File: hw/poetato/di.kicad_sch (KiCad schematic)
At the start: 10 parts, among them Q3 NTK3134N, U12 ISO1211

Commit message: hw: sync symbols with kicadlib field text and value updates
Update Symbols from Library for kicadlib 8686346 (field text 1.27 mm) and
5b35b6c (units on misc R/C values). Value text sizes synced to the library
by script, since a Value reset would also reset power-symbol net names.
Restored BOM_Entry Manufacturer/Part Number and the R57 Power field that the
update cleared, and field positions it reset. Nudged R1, C6, Q6 and C75 text
clear of the larger power-symbol labels. ERC clean, netlist unchanged apart
from the intended values.
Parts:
- R57: value 1k -> 1kΩ
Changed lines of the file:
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@@
 			(effects
 				(font
-					(size 1.524 1.524)
+					(size 1.27 1.27)
 				)
 				(justify left)
@@
 			(effects
 				(font
-					(size 1.524 1.524)
+					(size 1.27 1.27)
 				)
 				(justify left)
@@
 		(dnp no)
 		(fields_autoplaced yes)
-		(property "Reference" "#PWR094"
+		(property "Reference" "#PWR94"
 			(at 96.52 159.766 0)
 			(hide yes)
@@
 			(effects
 				(font
-					(size 0.508 0.508)
+					(size 1.27 1.27)
 				)
 			)
@@
 			(effects
 				(font
-					(size 0.762 0.762)
+					(size 1.27 1.27)
 				)
 			)
@@
 			(effects
 				(font
-					(size 1.524 1.524)
+					(size 1.27 1.27)
 				)
 			)
@@
 			(effects
 				(font
-					(size 1.524 1.524)
+					(size 1.27 1.27)
 				)
 			)
@@
 			(project "poetato"
 				(path "/f0f504bb-124c-46e5-ad39-032d3dfa78b3/7f50897c-81bd-4425-95ed-f5153c9db421/32a242c7-d9b1-4608-861e-d6aa3d0d20fd"
-					(reference "#PWR098")
+					(reference "#PWR98")
 					(unit 1)
 				)
 				(path "/f0f504bb-124c-46e5-ad39-032d3dfa78b3/7f50897c-81bd-4425-95ed-f5153c9db421/3e09c94c-e2ca-4383-a1d9-a605e5d78e01"
-					(reference "#PWR094")
+					(reference "#PWR94")
 					(unit 1)
 				)
 				(path "/f0f504bb-124c-46e5-ad39-032d3dfa78b3/7f50897c-81bd-4425-95ed-f5153c9db421/4efb7764-a312-4e2a-a696-e9a56a5b9d5e"
-					(reference "#PWR096")
+					(reference "#PWR96")
 					(unit 1)
 				)
@@
 		(in_pos_files yes)
 		(dnp no)
+		(fields_autoplaced yes)
 		(property "Reference" "R57"
 			(at 180.34 85.09 90)
@@
 			)
 		)
-		(property "Value" "1k"
+		(property "Value" "1kΩ"
 			(at 180.34 87.63 90)
 			(show_name no)
@@
 		(dnp no)
 		(fields_autoplaced yes)
-		(property "Reference" "#PWR0120"
+		(property "Reference" "#PWR120"
 			(at 96.52 88.646 0)
 			(hide yes)
@@
 			(effects
 				(font
-					(size 0.508 0.508)
+					(size 1.27 1.27)
 				)
 			)
@@
 			(effects
 				(font
-					(size 0.762 0.762)
+					(size 1.27 1.27)
 				)
 			)
@@
 			(effects
 				(font
-					(size 1.524 1.524)
+					(size 1.27 1.27)
 				)
 			)
@@
 			(effects
 				(font
-					(size 1.524 1.524)
+					(size 1.27 1.27)
 				)
 			)
@@
 			(project "poetato"
 				(path "/f0f504bb-124c-46e5-ad39-032d3dfa78b3/7f50897c-81bd-4425-95ed-f5153c9db421/32a242c7-d9b1-4608-861e-d6aa3d0d20fd"
-					(reference "#PWR0157")
+					(reference "#PWR157")
 					(unit 1)
 				)
 				(path "/f0f504bb-124c-46e5-ad39-032d3dfa78b3/7f50897c-81bd-4425-95ed-f5153c9db421/3e09c94c-e2ca-4383-a1d9-a605e5d78e01"
-					(reference "#PWR0120")
+					(reference "#PWR120")
 					(unit 1)
 				)
 				(path "/f0f504bb-124c-46e5-ad39-032d3dfa78b3/7f50897c-81bd-4425-95ed-f5153c9db421/4efb7764-a312-4e2a-a696-e9a56a5b9d5e"
-					(reference "#PWR0129")
+					(reference "#PWR129")
 					(unit 1)
 				)
@@
 			(effects
 				(font
-					(size 0.9906 0.9906)
+					(size 1.27 1.27)
 				)
 				(justify left)
@@
 			(effects
 				(font
-					(size 1.016 1.016)
+					(size 1.27 1.27)
 				)
 				(justify left)
@@
 			(effects
 				(font
-					(size 0.9906 0.9906)
+					(size 1.27 1.27)
 				)
 				(justify left)
@@
 		(dnp no)
 		(fields_autoplaced yes)
-		(property "Reference" "#PWR082"
+		(property "Reference" "#PWR82"
 			(at 111.76 106.426 0)
 			(hide yes)
@@
 			(effects
 				(font
-					(size 0.508 0.508)
+					(size 1.27 1.27)
 				)
 			)
@@
 			(effects
 				(font
-					(size 0.762 0.762)
+					(size 1.27 1.27)
 				)
 			)
@@
 			(effects
 				(font
-					(size 1.524 1.524)
+					(size 1.27 1.27)
 				)
 			)
@@
 			(effects
 				(font
-					(size 1.524 1.524)
+					(size 1.27 1.27)
 				)
 			)
@@
 			(project "poetato"
 				(path "/f0f504bb-124c-46e5-ad39-032d3dfa78b3/7f50897c-81bd-4425-95ed-f5153c9db421/32a242c7-d9b1-4608-861e-d6aa3d0d20fd"
-					(reference "#PWR084")
+					(reference "#PWR84")
 					(unit 1)
 				)
 				(path "/f0f504bb-124c-46e5-ad39-032d3dfa78b3/7f50897c-81bd-4425-95ed-f5153c9db421/3e09c94c-e2ca-4383-a1d9-a605e5d78e01"
-					(reference "#PWR082")
+					(reference "#PWR82")
 					(unit 1)
 				)
 				(path "/f0f504bb-124c-46e5-ad39-032d3dfa78b3/7f50897c-81bd-4425-95ed-f5153c9db421/4efb7764-a312-4e2a-a696-e9a56a5b9d5e"
-					(reference "#PWR083")
+					(reference "#PWR83")
 					(unit 1)
 				)
@@
 		(in_pos_files yes)
 		(dnp no)
+		(fields_autoplaced yes)
 		(property "Reference" "R54"
 			(at 154.94 84.328 90)
@@
 		(dnp no)
 		(fields_autoplaced yes)
-		(property "Reference" "#PWR095"
+		(property "Reference" "#PWR95"
 			(at 114.3 159.766 0)
 			(hide yes)
@@
 			(effects
 				(font
-					(size 0.508 0.508)
+					(size 1.27 1.27)
 				)
 			)
@@
 			(effects
 				(font
-					(size 0.762 0.762)
+					(size 1.27 1.27)
 				)
 			)
@@
 			(effects
 				(font
-					(size 1.524 1.524)
+					(size 1.27 1.27)
 				)
 			)
@@
 			(effects
 				(font
-					(size 1.524 1.524)
+					(size 1.27 1.27)
 				)
 			)
@@
 			(project "poetato"
 				(path "/f0f504bb-124c-46e5-ad39-032d3dfa78b3/7f50897c-81bd-4425-95ed-f5153c9db421/32a242c7-d9b1-4608-861e-d6aa3d0d20fd"
-					(reference "#PWR099")
+					(reference "#PWR99")
 					(unit 1)
 				)
 				(path "/f0f504bb-124c-46e5-ad39-032d3dfa78b3/7f50897c-81bd-4425-95ed-f5153c9db421/3e09c94c-e2ca-4383-a1d9-a605e5d78e01"
-					(reference "#PWR095")
+					(reference "#PWR95")
 					(unit 1)
 				)
 				(path "/f0f504bb-124c-46e5-ad39-032d3dfa78b3/7f50897c-81bd-4425-95ed-f5153c9db421/4efb7764-a312-4e2a-a696-e9a56a5b9d5e"
-					(reference "#PWR097")
+					(reference "#PWR97")
 					(unit 1)
 				)
@@
 		(dnp no)
 		(fields_autoplaced yes)
-		(property "Reference" "#PWR0100"
+		(property "Reference" "#PWR100"
 			(at 114.3 109.474 0)
 			(hide yes)
@@
 			(effects
 				(font
-					(size 0.508 0.508)
+					(size 1.27 1.27)
 				)
 			)
@@
 			(effects
 				(font
-					(size 0.762 0.762)
+					(size 1.27 1.27)
 				)
 				(justify left)
@@
 			(effects
 				(font
-					(size 1.524 1.524)
+					(size 1.27 1.27)
 				)
 			)
@@
 			(effects
 				(font
-					(size 1.524 1.524)
+					(size 1.27 1.27)
 				)
 			)
@@
 			(project "poetato"
 				(path "/f0f504bb-124c-46e5-ad39-032d3dfa78b3/7f50897c-81bd-4425-95ed-f5153c9db421/32a242c7-d9b1-4608-861e-d6aa3d0d20fd"
-					(reference "#PWR0102")
+					(reference "#PWR102")
 					(unit 1)
 				)
 				(path "/f0f504bb-124c-46e5-ad39-032d3dfa78b3/7f50897c-81bd-4425-95ed-f5153c9db421/3e09c94c-e2ca-4383-a1d9-a605e5d78e01"
-					(reference "#PWR0100")
+					(reference "#PWR100")
 					(unit 1)
 				)
 				(path "/f0f504bb-124c-46e5-ad39-032d3dfa78b3/7f50897c-81bd-4425-95ed-f5153c9db421/4efb7764-a312-4e2a-a696-e9a56a5b9d5e"
-					(reference "#PWR0101")
+					(reference "#PWR101")
 					(unit 1)
 				)
@@
 		(dnp no)
 		(fields_autoplaced yes)
-		(property "Reference" "#PWR0162"
+		(property "Reference" "#PWR162"
 			(at 96.52 63.754 0)
 			(hide yes)
@@
 			(effects
 				(font
-					(size 0.508 0.508)
+					(size 1.27 1.27)
 				)
 			)
@@
 			(effects
 				(font
-					(size 0.762 0.762)
+					(size 1.27 1.27)
 				)
 				(justify left)
@@
 			(effects
 				(font
-					(size 1.524 1.524)
+					(size 1.27 1.27)
 				)
 			)
@@
 			(effects
 				(font
-					(size 1.524 1.524)
+					(size 1.27 1.27)
 				)
 			)
@@
 			(project "poetato"
 				(path "/f0f504bb-124c-46e5-ad39-032d3dfa78b3/7f50897c-81bd-4425-95ed-f5153c9db421/32a242c7-d9b1-4608-861e-d6aa3d0d20fd"
-					(reference "#PWR0164")
+					(reference "#PWR164")
 					(unit 1)
 				)
 				(path "/f0f504bb-124c-46e5-ad39-032d3dfa78b3/7f50897c-81bd-4425-95ed-f5153c9db421/3e09c94c-e2ca-4383-a1d9-a605e5d78e01"
-					(reference "#PWR0162")
+					(reference "#PWR162")
 					(unit 1)
 				)
 				(path "/f0f504bb-124c-46e5-ad39-032d3dfa78b3/7f50897c-81bd-4425-95ed-f5153c9db421/4efb7764-a312-4e2a-a696-e9a56a5b9d5e"
-					(reference "#PWR0163")
-					(unit 1)
-				)
+					(reference "#PWR163")
+					(unit 1)
+				)

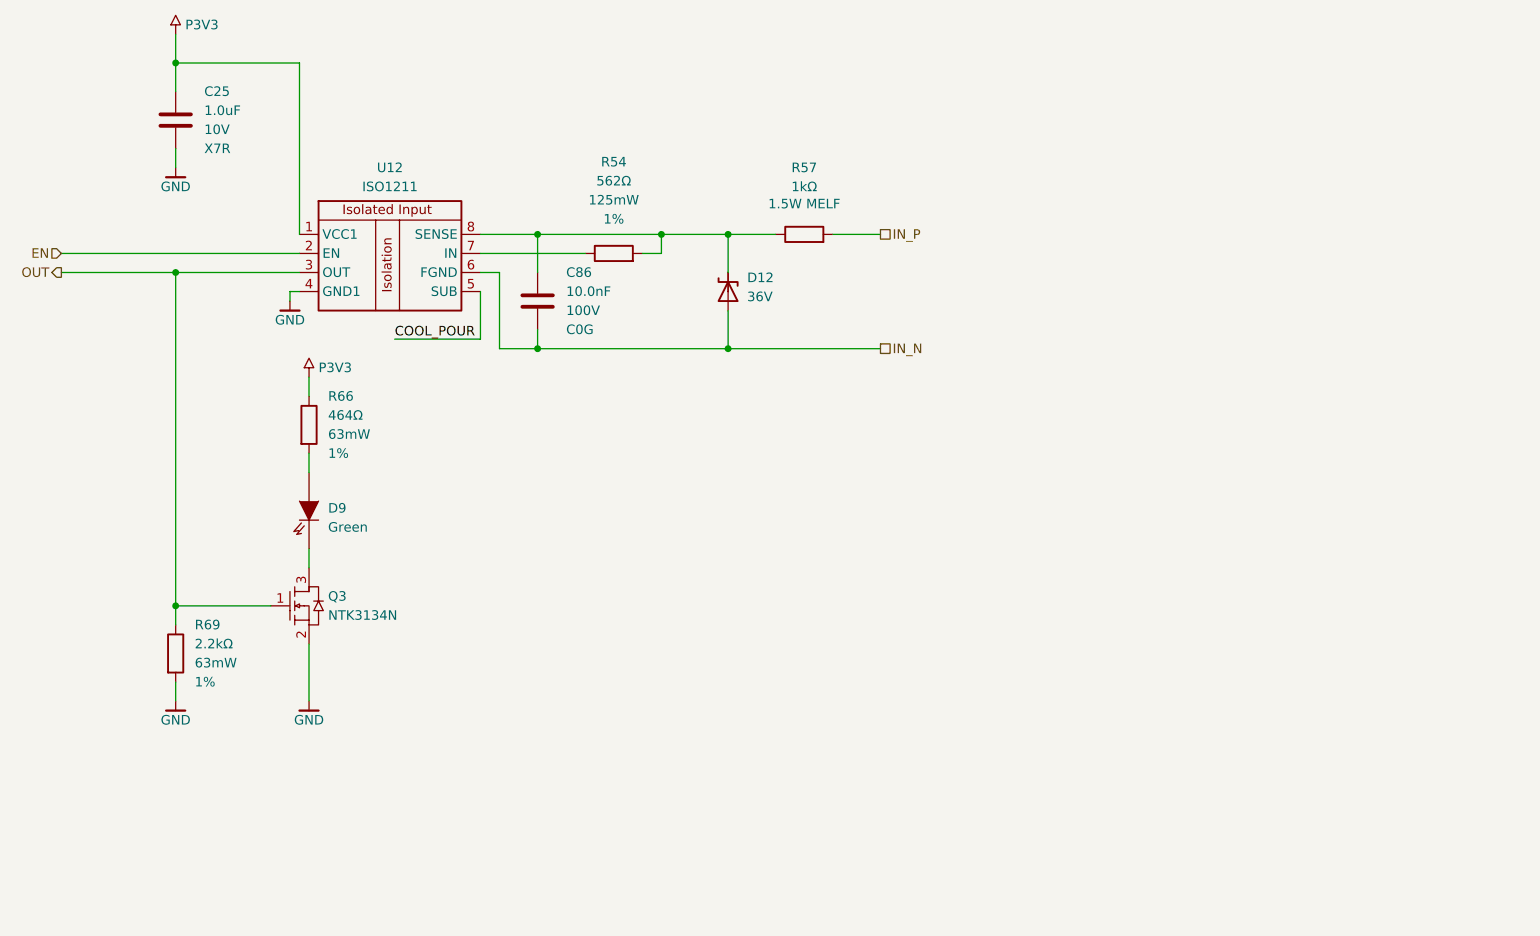
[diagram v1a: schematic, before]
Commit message: hw: 2.54 mm block titles, DI sheets on A3
- MCU: RTC block title at 2.54 mm (two lines); its contents move down
  7.62 mm to make room
- Peripherals: the three block titles at 2.54 mm, left-aligned in their frames
- DI: A3 like every other sheet, content placed as on the DO sheets; the
  COOL_POUR ERC exclusion in the project file follows the label

ERC clean, netlist unchanged.
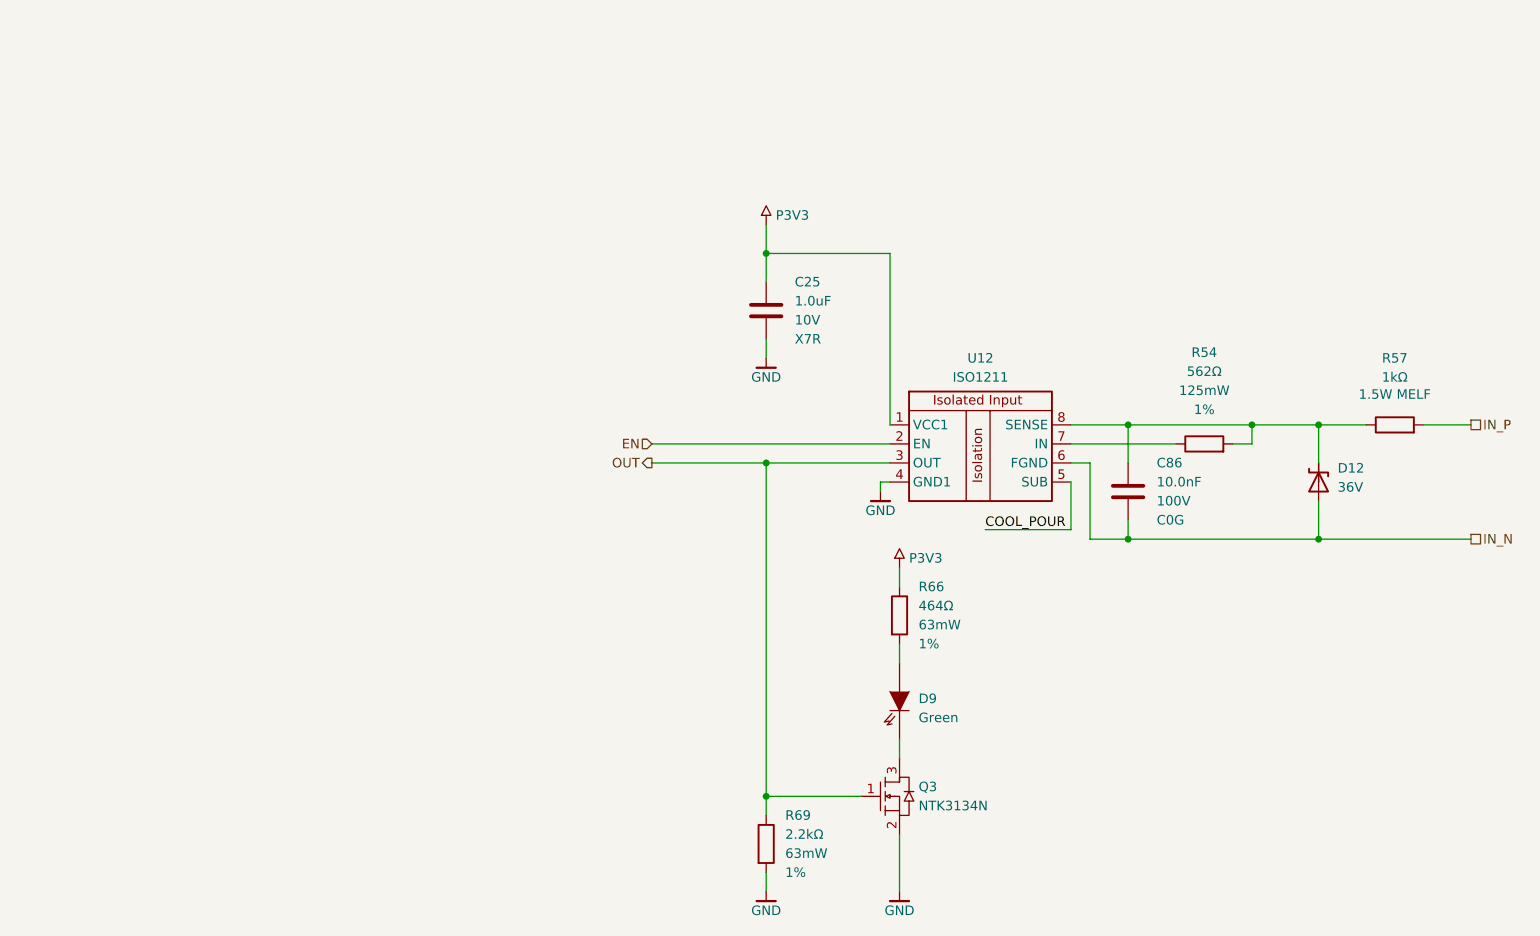
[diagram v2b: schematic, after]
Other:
- moved on the sheet: C25, C86, D12, D9, Q3, R54, R57, R66, R69, U12
